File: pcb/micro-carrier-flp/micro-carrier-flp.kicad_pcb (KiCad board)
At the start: 2 copper layers, 40.6 x 61 mm, 18 parts, among them J1 Conn_01x17, J2 Conn_01x17, U1 P4V-MINI, U10 P4V-MINI, U11 P4V-MINI, U12 P4V-MINI, U2 P4V-MINI, U3 P4V-MINI, U4 P4V-MINI, U5 P4V-MINI, U6 P4V-MINI, U7 P4V-MINI, U8 P4V-MINI, U9 P4V-MINI

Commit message: Add assembled headers
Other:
- board text added: "Micro Carrier V1.1B"
- board text removed: "Micro Carrier V1.1"

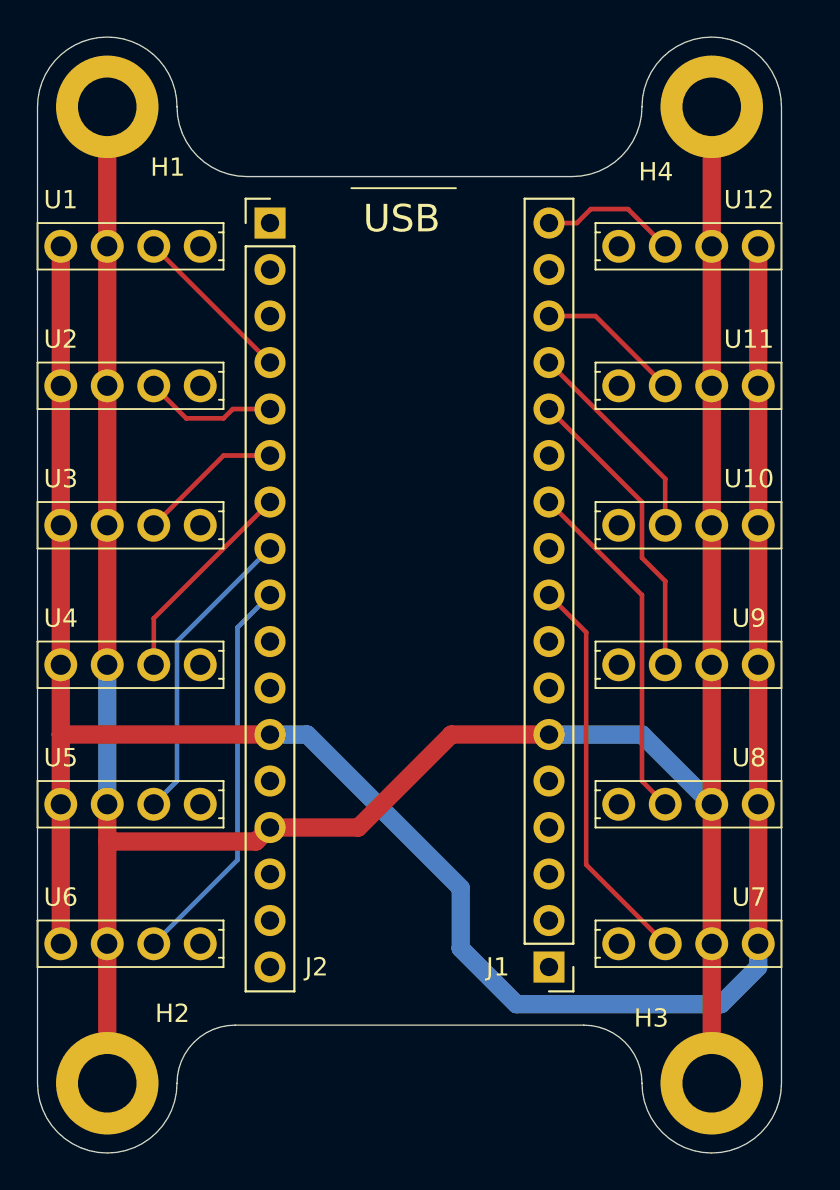
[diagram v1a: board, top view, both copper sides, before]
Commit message: Add micro analog refrence silkmask
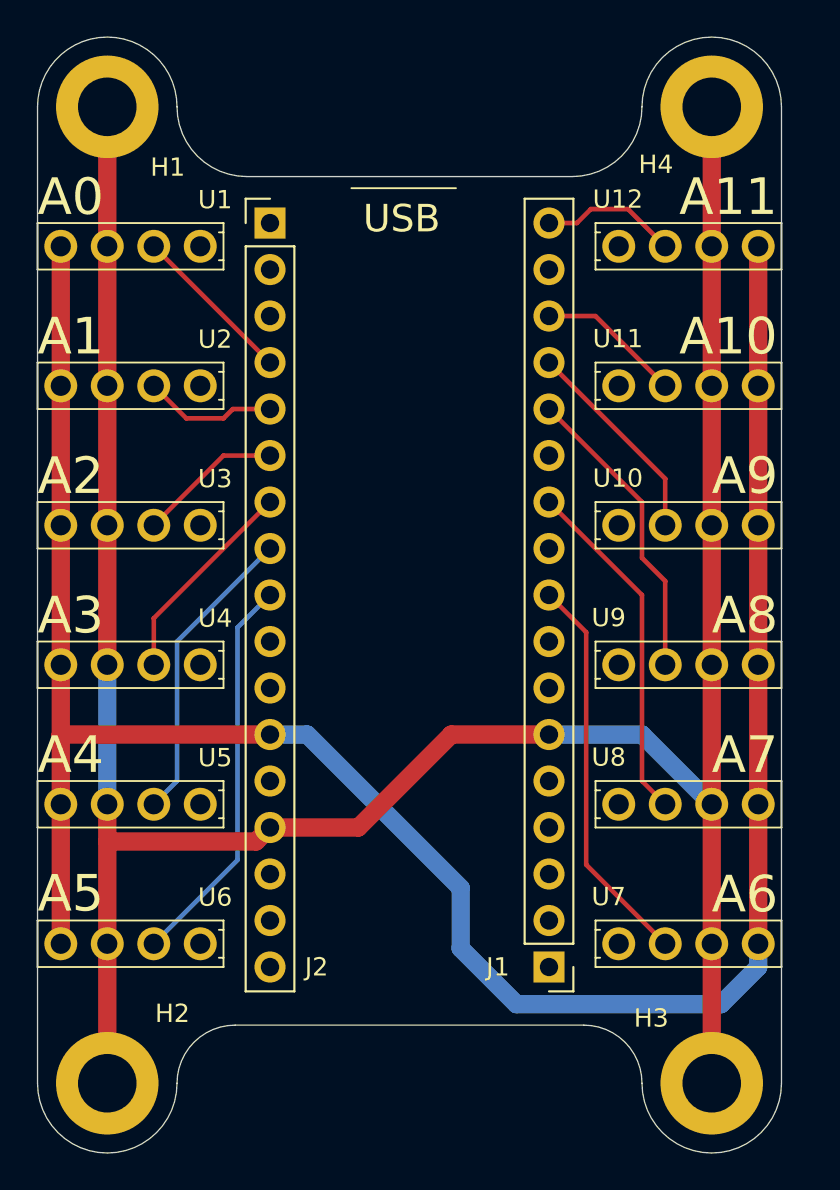
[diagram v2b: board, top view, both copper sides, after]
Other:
- board text added: "A0"
- board text added: "A1"
- board text added: "A10"
- board text added: "A11"
- board text added: "A2"
- board text added: "A3"
- board text added: "A4"
- board text added: "A5"
- board text added: "A6"
- board text added: "A7"
- board text added: "A8"
- board text added: "A9"
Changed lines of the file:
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@@
 		(at 146.05 100.33)
 		(property "Reference" "U9"
-			(at 7.112001 -2.54 0)
+			(at -0.549999 -2.57 0)
 			(unlocked yes)
 			(layer "F.SilkS")
@@
 		(at 123.19 115.57 180)
 		(property "Reference" "U6"
-			(at 7.62 2.54 0)
+			(at -0.81 2.54 0)
 			(unlocked yes)
 			(layer "F.SilkS")
@@
 		(at 146.05 92.71)
 		(property "Reference" "U10"
-			(at 7.112001 -2.54 0)
+			(at -0.05 -2.57 0)
 			(unlocked yes)
 			(layer "F.SilkS")
@@
 		(at 123.19 92.71 180)
 		(property "Reference" "U3"
-			(at 7.62 2.54 0)
+			(at -0.81 2.54 0)
 			(unlocked yes)
 			(layer "F.SilkS")
@@
 		(at 146.05 77.47)
 		(property "Reference" "U12"
-			(at 7.112 -2.54 0)
+			(at -0.050001 -2.57 0)
 			(unlocked yes)
 			(layer "F.SilkS")
@@
 		(at 146.05 85.09)
 		(property "Reference" "U11"
-			(at 7.112001 -2.54 0)
+			(at -0.05 -2.57 0)
 			(unlocked yes)
 			(layer "F.SilkS")
@@
 		(at 123.19 77.47 180)
 		(property "Reference" "U1"
-			(at 7.62 2.54 0)
+			(at -0.81 2.54 0)
 			(unlocked yes)
 			(layer "F.SilkS")
@@
 		(at 146.05 115.57)
 		(property "Reference" "U7"
-			(at 7.112 -2.54 0)
+			(at -0.55 -2.57 0)
 			(unlocked yes)
 			(layer "F.SilkS")
@@
 		(at 123.19 100.33 180)
 		(property "Reference" "U4"
-			(at 7.62 2.54 0)
+			(at -0.81 2.54 0)
 			(unlocked yes)
 			(layer "F.SilkS")
@@
 		(tags "mounting hole 3.2mm m3 din965")
 		(property "Reference" "H4"
-			(at -3.048 3.556 0)
+			(at -3.048 3.15 0)
 			(layer "F.SilkS")
 			(effects
@@
 		(at 123.19 107.95 180)
 		(property "Reference" "U5"
-			(at 7.62 2.54 0)
+			(at -0.81 2.54 0)
 			(unlocked yes)
 			(layer "F.SilkS")
@@
 		(at 146.05 107.95)
 		(property "Reference" "U8"
-			(at 7.112001 -2.54 0)
+			(at -0.549999 -2.57 0)
 			(unlocked yes)
 			(layer "F.SilkS")
@@
 		(at 123.19 85.09 180)
 		(property "Reference" "U2"
-			(at 7.62 2.54 0)
+			(at -0.81 2.54 0)
 			(unlocked yes)
 			(layer "F.SilkS")
@@
 		)
 	)
+	(gr_text "A5"
+		(at 114.3 114 0)
+		(layer "F.SilkS")
+		(effects
+			(font
+				(size 2 2)
+				(thickness 0.3)
+			)
+			(justify left bottom)
+		)
+	)
+	(gr_text "A7"
+		(at 151.13 106.426 0)
+		(layer "F.SilkS")
+		(effects
+			(font
+				(size 2 2)
+				(thickness 0.3)
+			)
+			(justify left bottom)
+		)
+	)
+	(gr_text "A11"
+		(at 149.352 75.946 0)
+		(layer "F.SilkS")
+		(effects
+			(font
+				(size 2 2)
+				(thickness 0.3)
+			)
+			(justify left bottom)
+		)
+	)
+	(gr_text "A6"
+		(at 151.13 114.046 0)
+		(layer "F.SilkS")
+		(effects
+			(font
+				(size 2 2)
+				(thickness 0.3)
+			)
+			(justify left bottom)
+		)
+	)
+	(gr_text "A2"
+		(at 114.3 91.186 0)
+		(layer "F.SilkS")
+		(effects
+			(font
+				(size 2 2)
+				(thickness 0.3)
+			)
+			(justify left bottom)
+		)
+	)
+	(gr_text "A3"
+		(at 114.3 98.806 0)
+		(layer "F.SilkS")
+		(effects
+			(font
+				(size 2 2)
+				(thickness 0.3)
+			)
+			(justify left bottom)
+		)
+	)
+	(gr_text "A8"
+		(at 151.13 98.806 0)
+		(layer "F.SilkS")
+		(effects
+			(font
+				(size 2 2)
+				(thickness 0.3)
+			)
+			(justify left bottom)
+		)
+	)
+	(gr_text "A4"
+		(at 114.3 106.426 0)
+		(layer "F.SilkS")
+		(effects
+			(font
+				(size 2 2)
+				(thickness 0.3)
+			)
+			(justify left bottom)
+		)
+	)
 	(gr_text "USB"
 		(at 132.08 76.835 0)
@@
 			)
 			(justify left bottom)
+		)
+	)
+	(gr_text "A9"
+		(at 151.13 91.186 0)
+		(layer "F.SilkS")
+		(effects
+			(font
+				(size 2 2)
+				(thickness 0.3)
+			)
+			(justify left bottom)
+		)
+	)
+	(gr_text "A1"
+		(at 114.3 83.566 0)
+		(layer "F.SilkS")
+		(effects
+			(font
+				(size 2 2)
+				(thickness 0.3)
+			)
+			(justify left bottom)
+		)
+	)
+	(gr_text "A0"
+		(at 114.3 75.946 0)
+		(layer "F.SilkS")
+		(effects
+			(font
+				(size 2 2)
+				(thickness 0.3)
+			)
+			(justify left bottom)
+		)
+	)
+	(gr_text "A10"
+		(at 149.352 83.566 0)
+		(layer "F.SilkS")
+		(effects
+			(font
+				(size 2 2)
+				(thickness 0.3)
+			)
+			(justify left bottom)
